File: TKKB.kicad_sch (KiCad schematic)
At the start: 38 parts, among them J1 UP, J2 DOWN, SW1 RESET, SW10 6, SW11 7, SW12 8, SW13 9, SW14 0, SW15 1, SW16 Q, SW17 W, SW18 E, SW19 R, SW2 REPEAT, SW20 T, SW21 Y, SW22 U, SW23 I, SW24 O, SW25 P, SW26 FIRE, SW27 FIRE, SW28 UP, SW29 DOWN, SW3 SPACE, SW30 RETURN, SW4 SPACE, SW5 SPACE, SW6 2, SW7 3, SW8 4, SW9 5

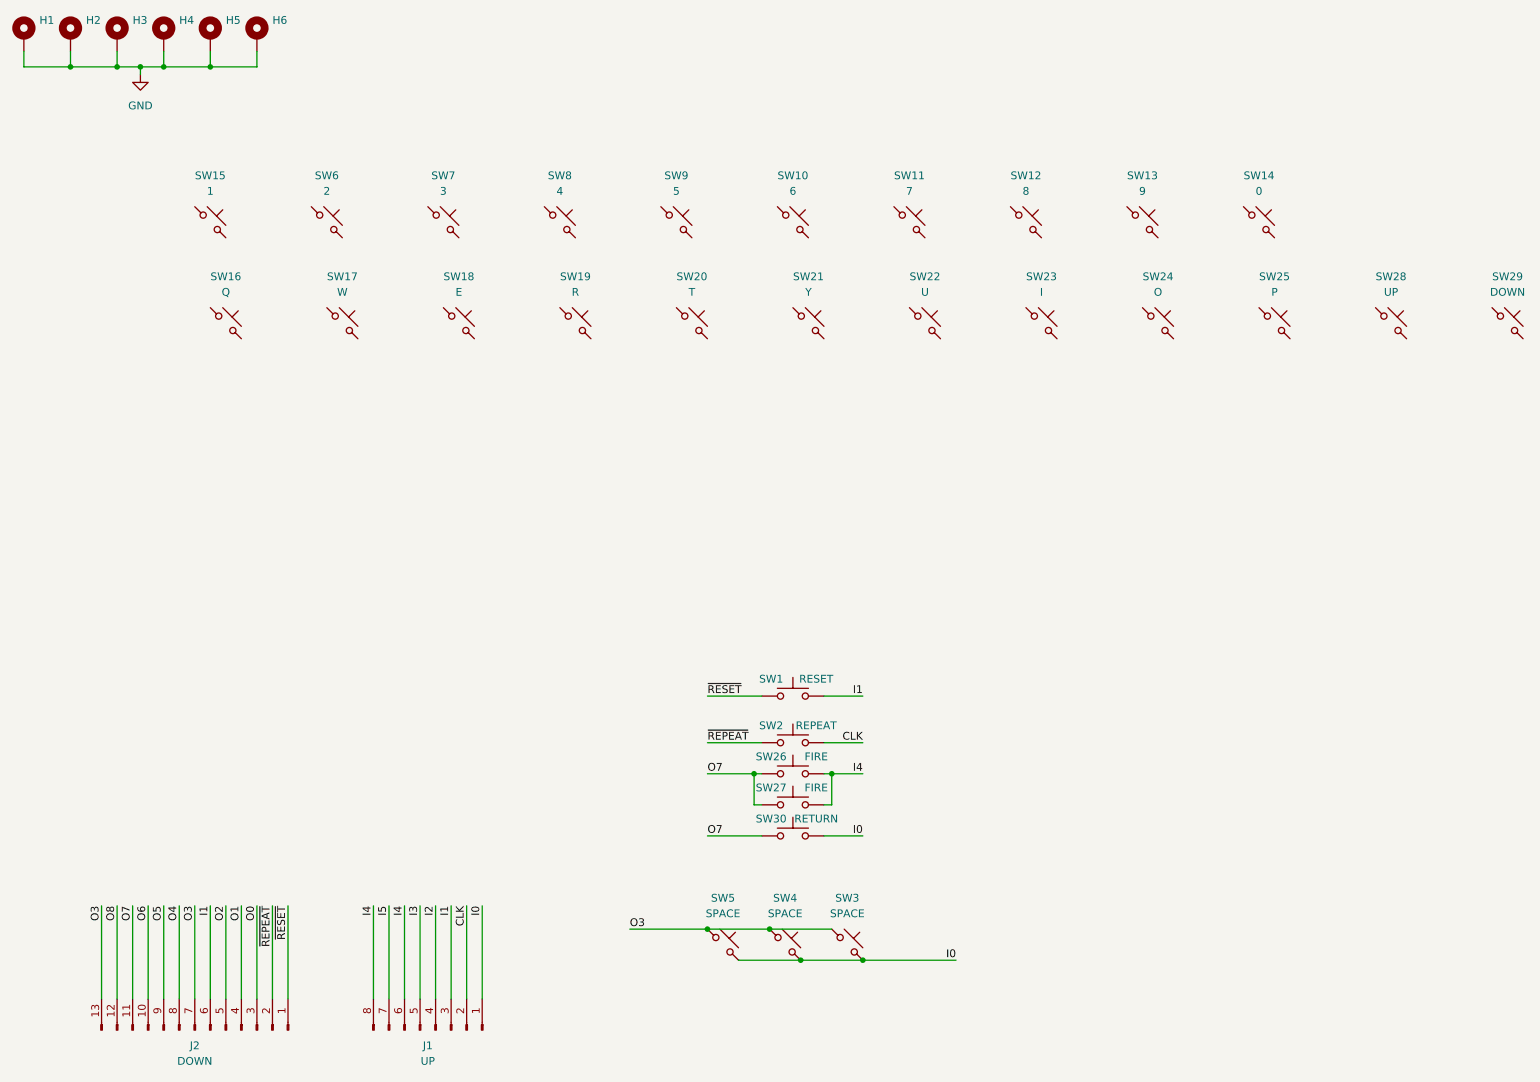
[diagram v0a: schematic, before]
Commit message: Add all keys to schematic
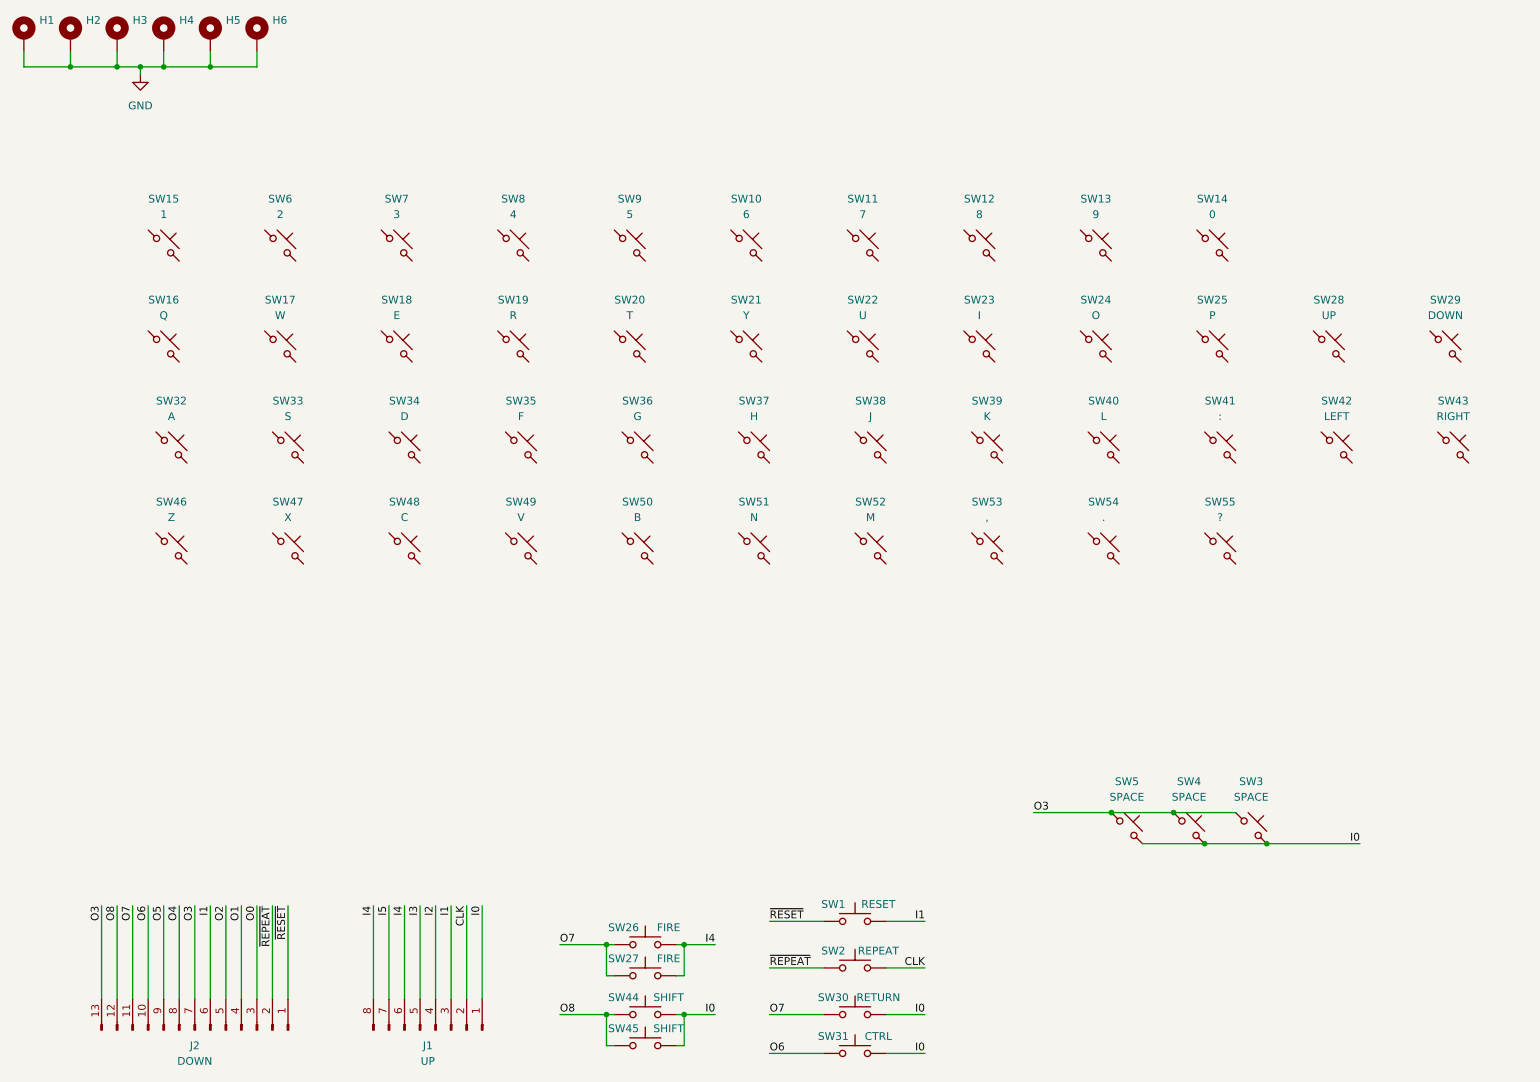
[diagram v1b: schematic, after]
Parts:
- added SW31: CTRL, symbol Switch:SW_Push
- added SW32: A, buttons:SW_Push_SMD_Large, symbol Switch:SW_Push_45deg
- added SW33: S, buttons:SW_Push_SMD_Large, symbol Switch:SW_Push_45deg
- added SW34: D, buttons:SW_Push_SMD_Large, symbol Switch:SW_Push_45deg
- added SW35: F, buttons:SW_Push_SMD_Large, symbol Switch:SW_Push_45deg
- added SW36: G, buttons:SW_Push_SMD_Large, symbol Switch:SW_Push_45deg
- added SW37: H, buttons:SW_Push_SMD_Large, symbol Switch:SW_Push_45deg
- added SW38: J, buttons:SW_Push_SMD_Large, symbol Switch:SW_Push_45deg
- added SW39: K, buttons:SW_Push_SMD_Large, symbol Switch:SW_Push_45deg
- added SW40: L, buttons:SW_Push_SMD_Large, symbol Switch:SW_Push_45deg
- added SW41: :, buttons:SW_Push_SMD_Large, symbol Switch:SW_Push_45deg
- added SW42: LEFT, buttons:SW_Push_SMD_Large, symbol Switch:SW_Push_45deg
- added SW43: RIGHT, buttons:SW_Push_SMD_Large, symbol Switch:SW_Push_45deg
- added SW44, SW45: SHIFT, symbol Switch:SW_Push
- added SW46: Z, buttons:SW_Push_SMD_Large, symbol Switch:SW_Push_45deg
- added SW47: X, buttons:SW_Push_SMD_Large, symbol Switch:SW_Push_45deg
- added SW48: C, buttons:SW_Push_SMD_Large, symbol Switch:SW_Push_45deg
- added SW49: V, buttons:SW_Push_SMD_Large, symbol Switch:SW_Push_45deg
- added SW50: B, buttons:SW_Push_SMD_Large, symbol Switch:SW_Push_45deg
- added SW51: N, buttons:SW_Push_SMD_Large, symbol Switch:SW_Push_45deg
- added SW52: M, buttons:SW_Push_SMD_Large, symbol Switch:SW_Push_45deg
- added SW53: ,, buttons:SW_Push_SMD_Large, symbol Switch:SW_Push_45deg
- added SW54: ., buttons:SW_Push_SMD_Large, symbol Switch:SW_Push_45deg
- added SW55: ?, buttons:SW_Push_SMD_Large, symbol Switch:SW_Push_45deg
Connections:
- net I0: now also SW31.2, SW44.2, SW45.2
- net O6: now also SW31.1
- net O8: now also SW44.1, SW45.1
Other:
- moved on the sheet: SW1, SW10, SW11, SW12, SW13, SW14, SW15, SW16, SW17, SW18, SW19, SW2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

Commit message: Completed drawing the keyboard matrix
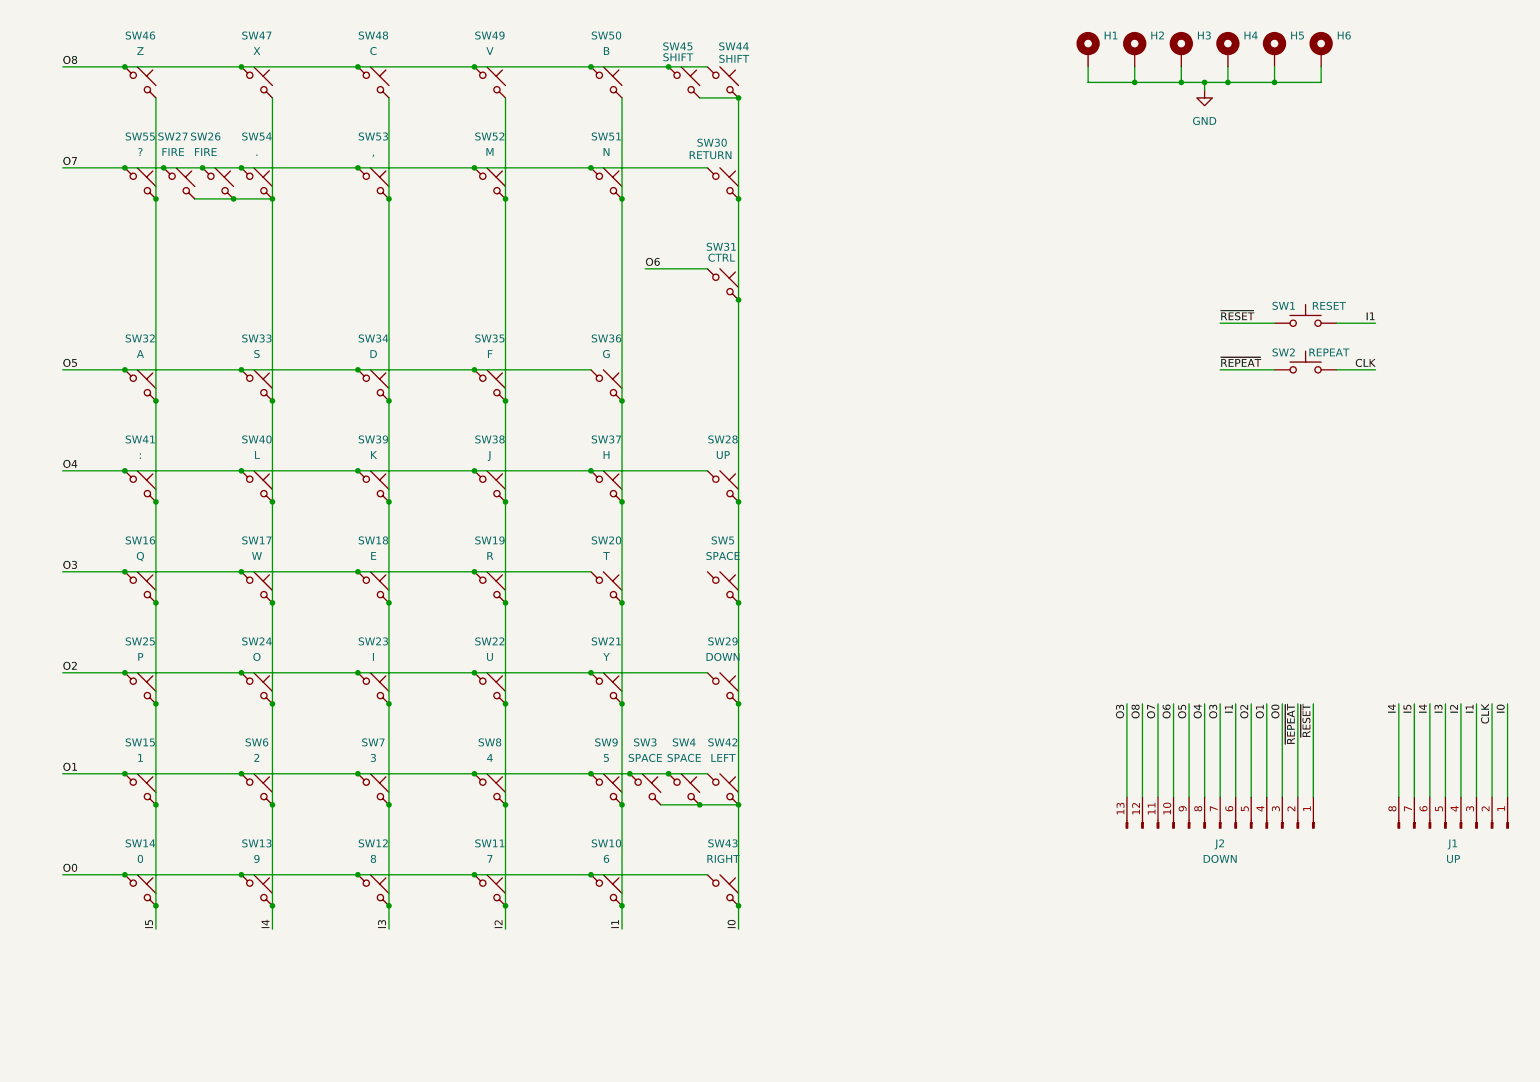
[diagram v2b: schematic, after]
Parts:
- SW26, SW27, SW30, SW31, SW44, SW45: symbol Switch:SW_Push -> Switch:SW_Push_45deg
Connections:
- net I0: now also SW28.2, SW29.2, SW42.2, SW43.2
- net I1: now also SW10.2, SW20.2, SW21.2, SW36.2, SW37.2, SW50.2, SW51.2, SW9.2
- net I2: now also SW11.2, SW19.2, SW22.2, SW35.2, SW38.2, SW49.2, SW52.2, SW8.2
- net I3: now also SW12.2, SW18.2, SW23.2, SW34.2, SW39.2, SW48.2, SW53.2, SW7.2
- net I4: now also SW13.2, SW17.2, SW24.2, SW33.2, SW40.2, SW47.2, SW54.2, SW6.2
- net I5: now also SW14.2, SW15.2, SW16.2, SW25.2, SW32.2, SW41.2, SW46.2, SW55.2
- net O0: now also SW10.1, SW11.1, SW12.1, SW13.1, SW14.1, SW43.1
- net O1: now also SW15.1, SW3.1, SW4.1, SW42.1, SW6.1, SW7.1, SW8.1, SW9.1
- net O2: now also SW21.1, SW22.1, SW23.1, SW24.1, SW25.1, SW29.1
- net O3: now also SW16.1, SW17.1, SW18.1, SW19.1, SW20.1; no longer SW3.1, SW4.1, SW5.1
- net O4: now also SW28.1, SW37.1, SW38.1, SW39.1, SW40.1, SW41.1
- net O5: now also SW32.1, SW33.1, SW34.1, SW35.1, SW36.1
- net O7: now also SW51.1, SW52.1, SW53.1, SW54.1, SW55.1
- net O8: now also SW46.1, SW47.1, SW48.1, SW49.1, SW50.1
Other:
- moved on the sheet: H1, H2, H3, H4, H5, H6, J1, J2, SW1, SW10, SW11, SW12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

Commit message: Begin drawing PCB
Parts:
- added D1: Power LED, LED_SMD:LED_1206_3216Metric_Pad1.42x1.75mm_HandSolder, symbol Device:LED_Small
- added J3: Power Connector, Connector_PinHeader_2.54mm:PinHeader_1x02_P2.54mm_Horizontal, symbol Connector:Conn_01x02_Pin
- J1: footprint Connector_PinHeader_2.54mm:PinHeader_1x08_P2.54mm_Vertical -> Connector_PinHeader_2.54mm:PinHeader_1x08_P2.54mm_Horizontal
- J2: footprint Connector_PinHeader_2.54mm:PinHeader_1x13_P2.54mm_Vertical -> Connector_PinHeader_2.54mm:PinHeader_1x13_P2.54mm_Horizontal
- SW1, SW2, SW26, SW27, SW30, SW31, SW44, SW45: footprint (none) -> buttons:SW_Push_SMD_Large
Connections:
- new net: D1.2 (A), J3.1 (Pin_1)
- new net: D1.1 (K), J3.2 (Pin_2)
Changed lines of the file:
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@@
 	(wire
 		(pts
+			(xy 215.9 93.98) (xy 237.49 93.98)
+		)
+		(stroke
+			(width 0)
+			(type default)
+		)
+	)
+	(wire
+		(pts
 			(xy 80.01 52.07) (xy 80.01 85.09)
 		)
@@
 	(wire
 		(pts
+			(xy 237.49 93.98) (xy 237.49 91.44)
+		)
+		(stroke
+			(width 0)
+			(type default)
+		)
+	)
+	(wire
+		(pts
 			(xy 93.98 80.01) (xy 113.03 80.01)
 		)
@@
 	(wire
 		(pts
+			(xy 215.9 91.44) (xy 227.33 91.44)
+		)
+		(stroke
+			(width 0)
+			(type default)
+		)
+	)
+	(wire
+		(pts
 			(xy 260.35 134.62) (xy 260.35 149.86)
 		)
@@
 	(wire
 		(pts
+			(xy 232.41 91.44) (xy 237.49 91.44)
+		)
+		(stroke
+			(width 0)
+			(type default)
+		)
+	)
+	(wire
+		(pts
 			(xy 119.38 146.05) (xy 125.73 146.05)
 		)
@@
 			)
 		)
-		(property "Footprint" "Connector_PinHeader_2.54mm:PinHeader_1x13_P2.54mm_Vertical"
+		(property "Footprint" "Connector_PinHeader_2.54mm:PinHeader_1x13_P2.54mm_Horizontal"
 			(at 215.9 154.94 0)
 			(effects
@@
 			)
 		)
-		(property "Footprint" ""
+		(property "Footprint" "buttons:SW_Push_SMD_Large"
 			(at 52.07 49.53 0)
 			(effects
@@
 			)
 		)
-		(property "Footprint" ""
+		(property "Footprint" "buttons:SW_Push_SMD_Large"
 			(at 134.62 49.53 0)
 			(effects
@@
 			)
 		)
-		(property "Footprint" ""
+		(property "Footprint" "buttons:SW_Push_SMD_Large"
 			(at 134.62 66.04 0)
 			(effects
@@
 			)
 		)
-		(property "Footprint" "Connector_PinHeader_2.54mm:PinHeader_1x08_P2.54mm_Vertical"
+		(property "Footprint" "Connector_PinHeader_2.54mm:PinHeader_1x08_P2.54mm_Horizontal"
 			(at 255.27 154.94 0)
 			(effects
@@
 			)
 		)
-		(property "Footprint" ""
+		(property "Footprint" "buttons:SW_Push_SMD_Large"
 			(at 128.27 33.02 0)
 			(effects
@@
 			)
 		)
-		(property "Footprint" ""
+		(property "Footprint" "buttons:SW_Push_SMD_Large"
 			(at 229.87 67.31 0)
 			(effects
@@
 			)
 		)
-		(property "Footprint" ""
+		(property "Footprint" "buttons:SW_Push_SMD_Large"
 			(at 229.87 74.93 0)
 			(effects
@@
 	)
 	(symbol
+		(lib_id "Connector:Conn_01x02_Pin")
+		(at 210.82 91.44 0)
+		(unit 1)
+		(exclude_from_sim no)
+		(in_bom yes)
+		(on_board yes)
+		(dnp no)
+		(fields_autoplaced yes)
+		(property "Reference" "J3"
+			(at 211.455 86.36 0)
+			(effects
+				(font
+					(size 1.27 1.27)
+				)
+			)
+		)
+		(property "Value" "Power Connector"
+			(at 211.455 88.9 0)
+			(effects
+				(font
+					(size 1.27 1.27)
+				)
+			)
+		)
+		(property "Footprint" "Connector_PinHeader_2.54mm:PinHeader_1x02_P2.54mm_Horizontal"
+			(at 210.82 91.44 0)
+			(effects
+				(font
+					(size 1.27 1.27)
+				)
+				(hide yes)
+			)
+		)
+		(property "Datasheet" "~"
+			(at 210.82 91.44 0)
+			(effects
+				(font
+					(size 1.27 1.27)
+				)
+				(hide yes)
+			)
+		)
+		(property "Description" "Generic connector, single row, 01x02, script generated"
+			(at 210.82 91.44 0)
+			(effects
+				(font
+					(size 1.27 1.27)
+				)
+				(hide yes)
+			)
+		)
+		(pin "2"
+		)
+		(pin "1"
+		)
+		(instances
+			(project ""
+				(path "/f9859692-ff17-45ca-b237-bba91b297170"
+					(reference "J3")
+					(unit 1)
+				)
+			)
+		)
+	)
+	(symbol
 		(lib_id "Mechanical:MountingHole_Pad")
 		(at 194.31 27.94 0)
@@
 			)
 		)
-		(property "Footprint" ""
+		(property "Footprint" "buttons:SW_Push_SMD_Large"
 			(at 134.62 33.02 0)
 			(effects
@@
 			)
 		)
-		(property "Footprint" ""
+		(property "Footprint" "buttons:SW_Push_SMD_Large"
 			(at 45.72 49.53 0)
 			(effects
@@
 					(unit 1)
 				)
+			)
+		)
+	)
+	(symbol
+		(lib_id "Device:LED_Small")
+		(at 229.87 91.44 0)
+		(mirror y)
+		(unit 1)
+		(exclude_from_sim no)
+		(in_bom yes)
+		(on_board yes)
+		(dnp no)
+		(property "Reference" "D1"
+			(at 229.8065 85.09 0)
+			(effects
+				(font
+					(size 1.27 1.27)
+				)
+			)
+		)
+		(property "Value" "Power LED"
+			(at 229.8065 87.63 0)
+			(effects
+				(font
+					(size 1.27 1.27)
+				)
+			)
+		)
+		(property "Footprint" "LED_SMD:LED_1206_3216Metric_Pad1.42x1.75mm_HandSolder"
+			(at 229.87 91.44 90)
+			(effects
+				(font
+					(size 1.27 1.27)
+				)
+				(hide yes)
+			)
+		)
+		(property "Datasheet" "~"
+			(at 229.87 91.44 90)
+			(effects
+				(font
+					(size 1.27 1.27)
+				)
+				(hide yes)
+			)
+		)
+		(property "Description" "Light emitting diode, small symbol"
+			(at 229.87 91.44 0)
+			(effects
+				(font
+					(size 1.27 1.27)
+				)
+				(hide yes)
+			)
+		)
+		(property "Sim.Pin" "1=K 2=A"
+			(at 229.87 91.44 0)
+			(effects
+				(font
+					(size 1.27 1.27)
+				)
+				(hide yes)
+			)
+		)
+		(pin "1"
+		)
+		(pin "2"
+		)
+		(instances
+			(project ""
+				(path "/f9859692-ff17-45ca-b237-bba91b297170"
+					(reference "D1")
+					(unit 1)
+				)
